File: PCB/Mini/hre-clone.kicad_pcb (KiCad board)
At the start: 2 copper layers, 103 x 73.1 mm, 23 parts, among them SW1 SW_DIP_x04, U1 74LS258, U10 MC6845, U11 MC6845, U12 DIL14, U13 7402, U2 74LS174, U3 74LS257, U4 74LS244, U5 2716, U6 2716, U7 74LS05, U8 74LS155, U9 74LS257

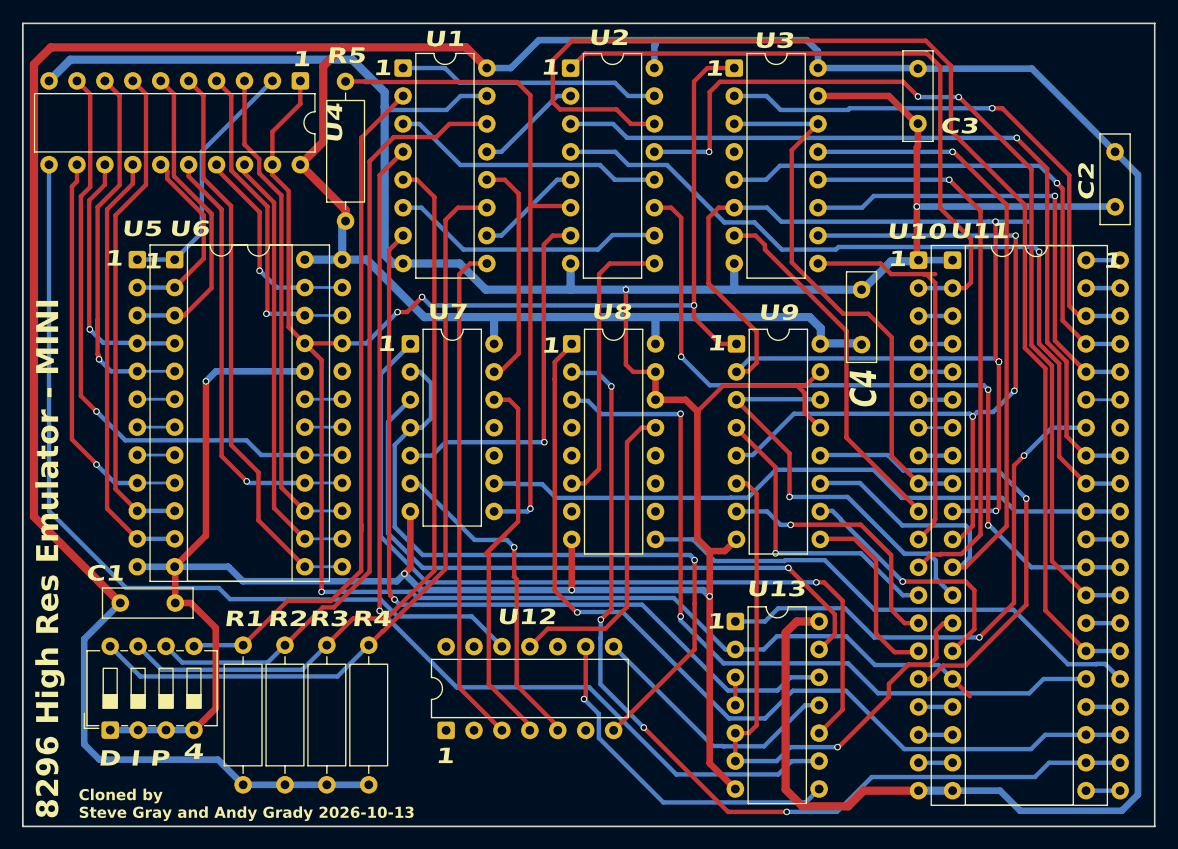
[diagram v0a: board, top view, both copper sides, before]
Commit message: Even more Mini!
Shuffled some chips and traces, added beveled corners and made the text labelling more normal.
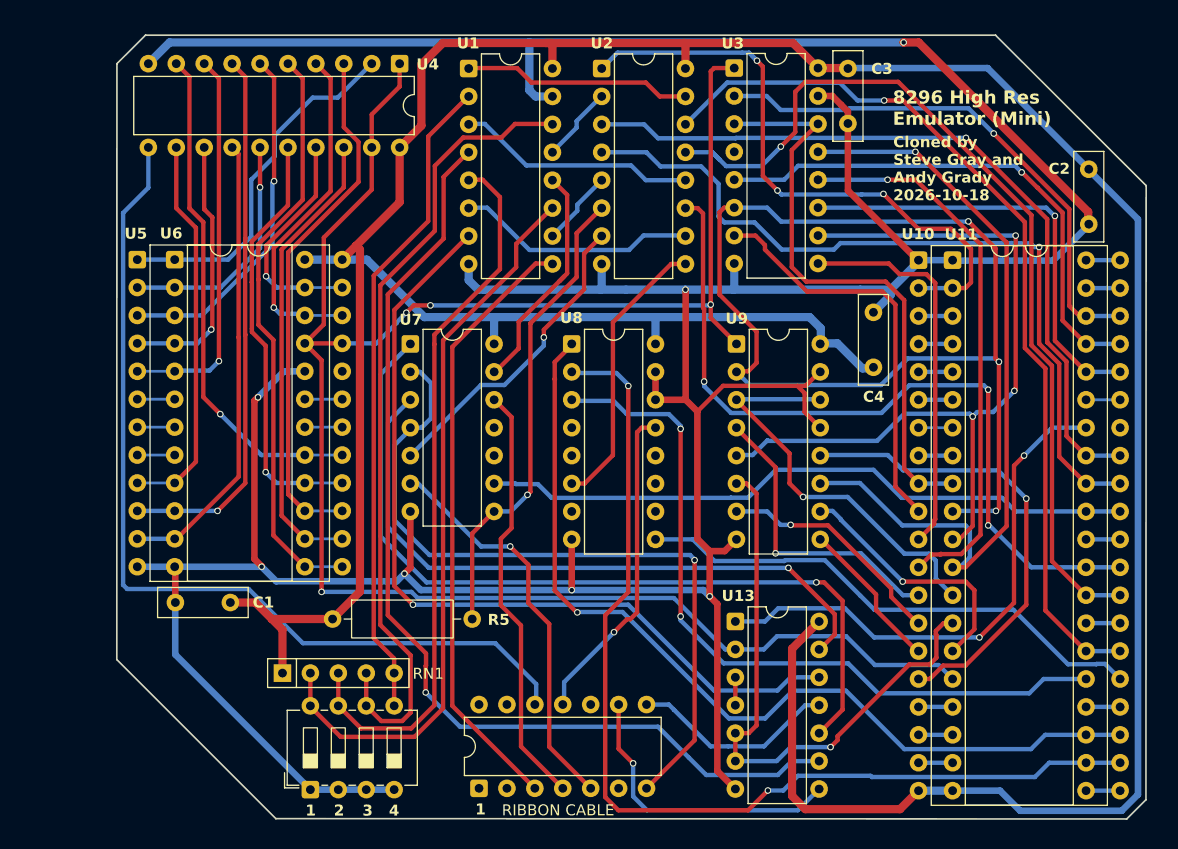
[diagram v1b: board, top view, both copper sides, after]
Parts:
- removed R1, R2, R3, R4: R, Resistor_THT:R_Axial_DIN0309_L9.0mm_D3.2mm_P12.70mm_Horizontal
- added RN1: 3300 ohm, Resistor_THT:R_Array_SIP5, F.Cu at (151.8, 139.5)
- R5: value R -> 3300
- moved R5 36.2 mm to (156.4, 134.6), turned to 0 degrees
- moved SW1 19.0 mm to (154.4, 150.1)
- moved C1 10.0 mm to (147.1, 133.1), turned to 180 degrees
- moved U4 9.17 mm to (162.5, 84.1)
- moved C3 6.37 mm to (203.3, 84.5)
- moved U12 6.06 mm to (169.7, 150.0)
- moved U1 5.97 mm to (168.8, 84.5)
- moved C2 2.87 mm to (225.2, 93.7)
- moved U2 2.83 mm to (180.9, 84.5)
- moved C4 2.33 mm to (205.6, 111.7)
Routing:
- net VCC: track 396.6 -> 316.9 mm, vias 1 -> 0
- net GND: track 347.1 -> 380.2 mm, vias 6 -> 7
- net D7: track 113.2 -> 82.1 mm, vias 0 -> 1
- net Net-(U2-D2): track 62.0 -> 43.1 mm
- net XA7: track 23.3 -> 32.8 mm, vias 1 -> 0
- net Q7: track 55.5 -> 46.2 mm
- net MUX3D: track 46.5 -> 55.5 mm
- net R/~{W}: track 85.6 -> 93.2 mm, vias 4 -> 2
- net ~{LATCH2}: track 30.6 -> 36.5 mm
- net D0: track 75.7 -> 70.2 mm
- net RIBBON-12: track 78.0 -> 83.4 mm
- net RIBBON-8: track 24.0 -> 18.8 mm
- net Net-(U2-Q2): track 33.5 -> 28.4 mm
- net RIBBON-9: track 31.9 -> 27.2 mm
- net MA6: track 102.3 -> 97.7 mm, vias 4 -> 3
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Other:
- board size 103 x 73.1 mm -> 93.6 x 71.3 mm
- board text added: "2"
- board text added: "3"
- board text added: "8296 High Res Emulator (Mini)"
- board text added: "Cloned by Steve Gray and Andy Grady 2026-10-18"
- board text added: "RIBBON CABLE"
- board text removed: "324891-01"
- board text removed: "8296 High Res Emulator - MINI"
- board text removed: "Cloned by Steve Gray and Andy Grady 2026-10-13"
- board text removed: "D I P"
- board text removed: "FAB"
- board text removed: "NO"
- board text removed: "REV B"
